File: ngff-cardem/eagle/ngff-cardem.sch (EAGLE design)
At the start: 143 parts, among them IC201 CB3Q3244PW, IC202 CB3Q3244PW, IC203 IP4234CZ6, IC204 FPF2109, IC205 FPF2109, IC301 TPS22958N-DGN, IC302 TPS22958N-DGK, J301 PJ-002BH-SMT-TR, M2 MENTOR_12701001, M3 MENTOR_12701001, Q201 12MHz, T101 BC850, T102 BC850, U201 IP4234CZ6, U202 AT91SAM3S-AU, U301 MIC5366-1.8YC5, X101 PINHD-2X3-SP, X102 ZX360D-B-10P(30), X201 MINI-USB-SHIELD-UX60-MB-5ST, X202 2.54mm, X203 JACK2.5_SJ-2523, X301 171826-4-RA

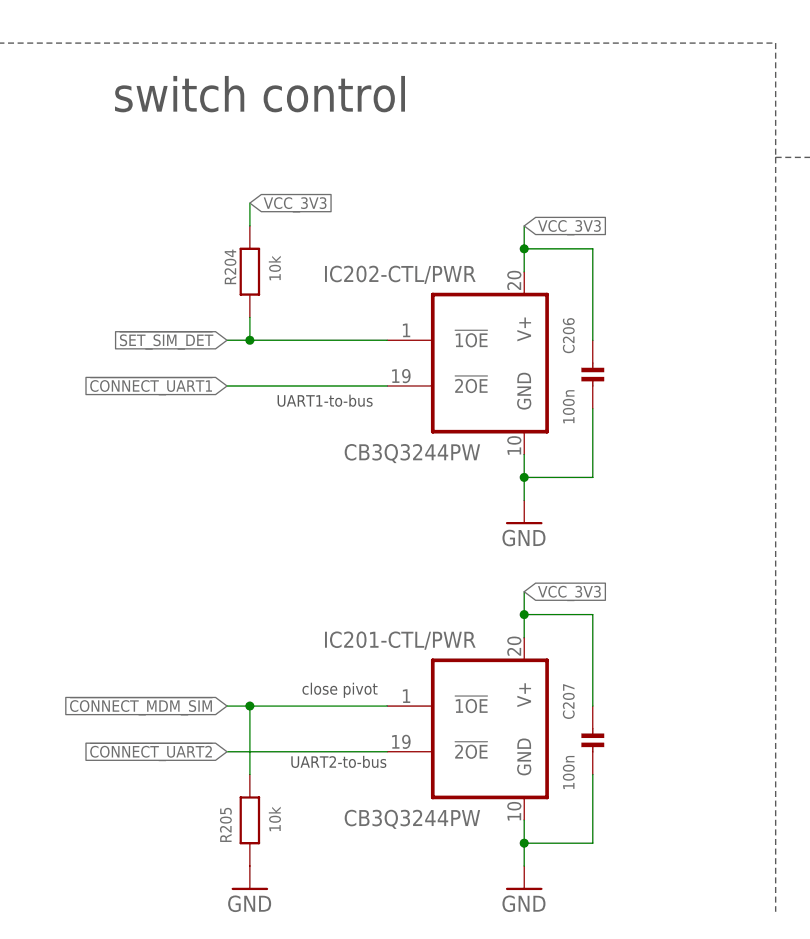
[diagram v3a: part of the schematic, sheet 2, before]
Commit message: ngff-cardem: insert 2 PUs as DNP for possible !CONNECT_UART{1,2} biasing
solves SYS#5532
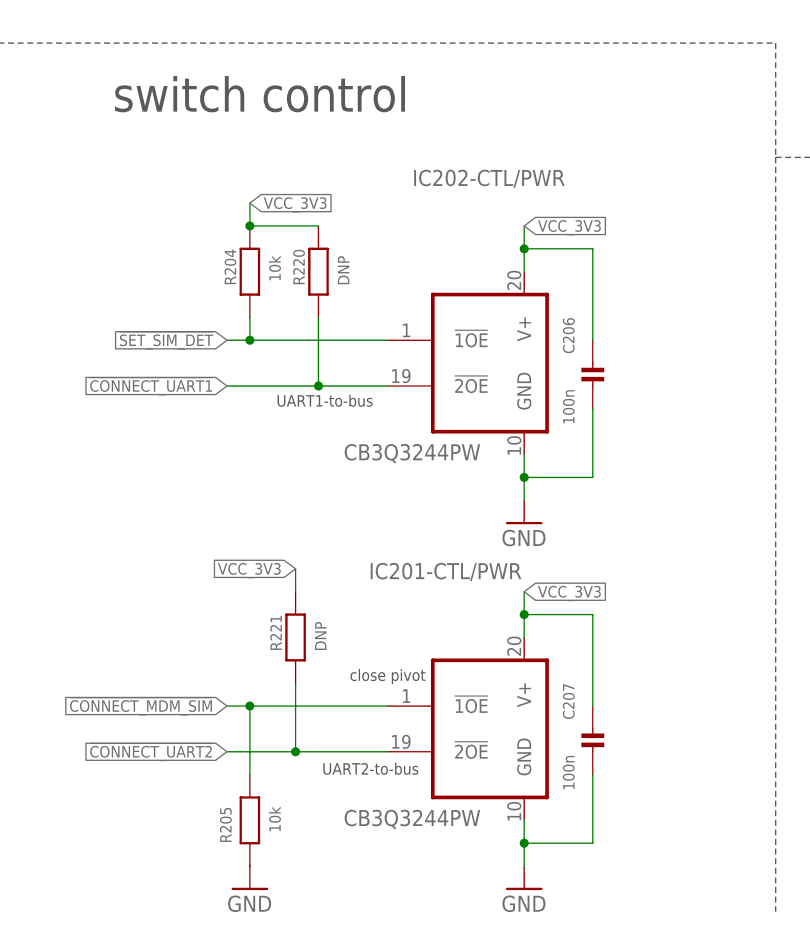
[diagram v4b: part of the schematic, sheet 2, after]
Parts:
- added R220, R221: DNP, rc-sysmocom:RESISTOR_0603
- X201: DESCRIPTION (none) -> NO DESCRIPTION; MANUFACTURER (none) -> UNKNOWN MANUFACTURER; MANUFACTURERPARTNUMBER (none) -> UNKNOWN MANUFACTURER PART NUMBER; ROHSCERTIFICATE (none) -> UNKNOWN ROHS CERTIFICATE; SOURCEPARTNUMBER (none) -> UNKNOWN SOURCE PART NUMBER
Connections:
- net !CONNECT_UART1: now also R220.2
- net !CONNECT_UART2: now also R221.2
- net VCC_3V3: now also R220.1, R221.1
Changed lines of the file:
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@@
 <part name="X201" library="con-hirose" deviceset="MINI-USB-SHIELD-" device="UX60-MB-5ST">
 <attribute name="CLASS" value="CONNECTOR"/>
-<attribute name="DESCRIPTION" value=""/>
+<attribute name="DESCRIPTION" value="NO DESCRIPTION"/>
 <attribute name="LINK" value="http://www.digikey.com/product-detail/en/hirose-electric-co-ltd/UX60-MB-5ST/H2959CT-ND/597538"/>
-<attribute name="MANUFACTURER" value=""/>
-<attribute name="MANUFACTURERPARTNUMBER" value=""/>
+<attribute name="MANUFACTURER" value="UNKNOWN MANUFACTURER"/>
+<attribute name="MANUFACTURERPARTNUMBER" value="UNKNOWN MANUFACTURER PART NUMBER"/>
 <attribute name="OC_FARNELL" value=""/>
 <attribute name="OC_NEWARK" value=""/>
 <attribute name="POPULATED" value="TRUE"/>
-<attribute name="ROHSCERTIFICATE" value=""/>
+<attribute name="ROHSCERTIFICATE" value="UNKNOWN ROHS CERTIFICATE"/>
 <attribute name="SOURCE" value="DIGIKEY"/>
-<attribute name="SOURCEPARTNUMBER" value=""/>
+<attribute name="SOURCEPARTNUMBER" value="UNKNOWN SOURCE PART NUMBER"/>
 </part>
 <part name="U201" library="laforge" deviceset="IP4234CZ6" device="">
@@
 <attribute name="SOURCEPARTNUMBER" value="UNKNOWN SOURCE PART NUMBER"/>
 </part>
+<part name="R220" library="rc-sysmocom" deviceset="RESISTOR" device="_0603" value="DNP">
+<attribute name="CLASS" value="RESISTOR"/>
+<attribute name="DESCRIPTION" value="NO DESCRIPTION"/>
+<attribute name="LINK" value="UNKNOWN LINK"/>
+<attribute name="MANUFACTURER" value="UNKNOWN MANUFACTURER"/>
+<attribute name="MANUFACTURERPARTNUMBER" value="UNKNOWN MANUFACTURER PART NUMBER"/>
+<attribute name="POPULATED" value="FALSE"/>
+<attribute name="ROHSCERTIFICATE" value="UNKNOWN ROHS CERTIFICATE"/>
+<attribute name="SOURCE" value="UNKNOWN SOURCE"/>
+<attribute name="SOURCEPARTNUMBER" value="UNKNOWN SOURCE PART NUMBER"/>
+</part>
+<part name="R221" library="rc-sysmocom" deviceset="RESISTOR" device="_0603" value="DNP">
+<attribute name="CLASS" value="RESISTOR"/>
+<attribute name="DESCRIPTION" value="NO DESCRIPTION"/>
+<attribute name="LINK" value="UNKNOWN LINK"/>
+<attribute name="MANUFACTURER" value="UNKNOWN MANUFACTURER"/>
+<attribute name="MANUFACTURERPARTNUMBER" value="UNKNOWN MANUFACTURER PART NUMBER"/>
+<attribute name="POPULATED" value="FALSE"/>
+<attribute name="ROHSCERTIFICATE" value="UNKNOWN ROHS CERTIFICATE"/>
+<attribute name="SOURCE" value="UNKNOWN SOURCE"/>
+<attribute name="SOURCEPARTNUMBER" value="UNKNOWN SOURCE PART NUMBER"/>
+</part>
 </parts>
 <sheets>
@@
 <text x="137.16" y="81.28" size="3.81" layer="97" ratio="10">switch bank</text>
 <text x="82.296" y="62.484" size="1.27" layer="97" rot="R180">UART1-to-bus</text>
-<text x="83.82" y="22.352" size="1.27" layer="97" rot="R180">UART2-to-bus</text>
-<text x="82.804" y="30.48" size="1.27" layer="97" rot="R180">close pivot</text>
+<text x="87.376" y="21.59" size="1.27" layer="97" rot="R180">UART2-to-bus</text>
+<text x="88.138" y="32.004" size="1.27" layer="97" rot="R180">close pivot</text>
 <wire x1="251.46" y1="88.9" x2="330.2" y2="88.9" width="0.1524" layer="97" style="longdash"/>
 <wire x1="134.62" y1="50.8" x2="325.12" y2="50.8" width="0.1016" layer="97" style="dashdot"/>
@@
 <instance part="GND7" gate="1" x="119.38" y="223.52" rot="R270"/>
 <instance part="GND8" gate="1" x="119.38" y="218.44" rot="R270"/>
-<instance part="IC202" gate="-CTL/PWR" x="93.98" y="66.04"/>
+<instance part="IC202" gate="-CTL/PWR" x="93.98" y="66.04" smashed="yes">
+<attribute name="NAME" x="86.614" y="85.725" size="1.778" layer="95"/>
+<attribute name="VALUE" x="94.234" y="57.023" size="1.778" layer="96" rot="R180"/>
+</instance>
 <instance part="IC202" gate="-1OE_4" x="190.5" y="10.16"/>
 <instance part="IC202" gate="-2OE_1" x="160.02" y="55.88" smashed="yes" rot="MR180">
@@
 <attribute name="NAME" x="155.702" y="48.387" size="1.778" layer="95" rot="R180"/>
 </instance>
-<instance part="IC201" gate="-CTL/PWR" x="93.98" y="25.4"/>
+<instance part="IC201" gate="-CTL/PWR" x="93.98" y="25.4" smashed="yes">
+<attribute name="NAME" x="98.806" y="43.815" size="1.778" layer="95" rot="R180"/>
+<attribute name="VALUE" x="94.234" y="16.383" size="1.778" layer="96" rot="R180"/>
+</instance>
 <instance part="IC201" gate="-1OE_2" x="198.12" y="43.18" smashed="yes">
 <attribute name="NAME" x="198.882" y="49.657" size="1.778" layer="95" rot="R180"/>
@@
 <attribute name="VALUE" x="70.739" y="77.978" size="1.27" layer="96" rot="R270"/>
 </instance>
+<instance part="R220" gate="G$1" x="76.2" y="76.2" smashed="yes" rot="R270">
+<attribute name="NAME" x="73.406" y="78.74" size="1.27" layer="95" rot="R270"/>
+<attribute name="VALUE" x="78.359" y="77.978" size="1.27" layer="96" rot="R270"/>
+<attribute name="DESCRIPTION" x="76.2" y="76.2" size="1.778" layer="96" rot="R270" display="off"/>
+<attribute name="MANUFACTURER" x="76.2" y="76.2" size="1.778" layer="96" rot="R270" display="off"/>
+<attribute name="MANUFACTURERPARTNUMBER" x="76.2" y="76.2" size="1.778" layer="96" rot="R270" display="off"/>
+<attribute name="SOURCE" x="76.2" y="76.2" size="1.778" layer="96" rot="R270" display="off"/>
+<attribute name="SOURCEPARTNUMBER" x="76.2" y="76.2" size="1.778" layer="96" rot="R270" display="off"/>
+<attribute name="ROHSCERTIFICATE" x="76.2" y="76.2" size="1.778" layer="96" rot="R270" display="off"/>
+<attribute name="POPULATED" x="76.2" y="76.2" size="1.778" layer="96" rot="R270" display="off"/>
+<attribute name="CLASS" x="76.2" y="76.2" size="1.778" layer="96" rot="R270" display="off"/>
+<attribute name="LINK" x="76.2" y="76.2" size="1.778" layer="96" rot="R270" display="off"/>
+</instance>
+<instance part="R221" gate="G$1" x="73.66" y="35.56" smashed="yes" rot="R270">
+<attribute name="NAME" x="70.866" y="38.1" size="1.27" layer="95" rot="R270"/>
+<attribute name="VALUE" x="75.819" y="37.338" size="1.27" layer="96" rot="R270"/>
+<attribute name="DESCRIPTION" x="73.66" y="35.56" size="1.778" layer="96" rot="R270" display="off"/>
+<attribute name="MANUFACTURER" x="73.66" y="35.56" size="1.778" layer="96" rot="R270" display="off"/>
+<attribute name="MANUFACTURERPARTNUMBER" x="73.66" y="35.56" size="1.778" layer="96" rot="R270" display="off"/>
+<attribute name="SOURCE" x="73.66" y="35.56" size="1.778" layer="96" rot="R270" display="off"/>
+<attribute name="SOURCEPARTNUMBER" x="73.66" y="35.56" size="1.778" layer="96" rot="R270" display="off"/>
+<attribute name="ROHSCERTIFICATE" x="73.66" y="35.56" size="1.778" layer="96" rot="R270" display="off"/>
+<attribute name="POPULATED" x="73.66" y="35.56" size="1.778" layer="96" rot="R270" display="off"/>
+<attribute name="CLASS" x="73.66" y="35.56" size="1.778" layer="96" rot="R270" display="off"/>
+<attribute name="LINK" x="73.66" y="35.56" size="1.778" layer="96" rot="R270" display="off"/>
+</instance>
 </instances>
 <busses>
@@
 <label x="66.04" y="63.5" size="1.27" layer="95" rot="R180" xref="yes"/>
 <pinref part="IC202" gate="-CTL/PWR" pin="!2OE"/>
-<wire x1="83.82" y1="63.5" x2="66.04" y2="63.5" width="0.1524" layer="91"/>
+<wire x1="83.82" y1="63.5" x2="76.2" y2="63.5" width="0.1524" layer="91"/>
+<pinref part="R220" gate="G$1" pin="2"/>
+<wire x1="76.2" y1="63.5" x2="66.04" y2="63.5" width="0.1524" layer="91"/>
+<wire x1="76.2" y1="71.12" x2="76.2" y2="63.5" width="0.1524" layer="91"/>
+<junction x="76.2" y="63.5"/>
 </segment>
 <segment>
@@
 <wire x1="68.58" y1="81.28" x2="68.58" y2="83.82" width="0.1524" layer="91"/>
 <label x="68.58" y="83.82" size="1.27" layer="95" xref="yes"/>
+<pinref part="R220" gate="G$1" pin="1"/>
+<wire x1="76.2" y1="81.28" x2="68.58" y2="81.28" width="0.1524" layer="91"/>
+<junction x="68.58" y="81.28"/>
 </segment>
 <segment>
@@
 <label x="30.48" y="66.04" size="1.27" layer="95" rot="R90" xref="yes"/>
 </segment>
+<segment>
+<label x="73.66" y="43.18" size="1.27" layer="95" rot="R180" xref="yes"/>
+<pinref part="R221" gate="G$1" pin="1"/>
+<wire x1="73.66" y1="43.18" x2="73.66" y2="40.64" width="0.1524" layer="91"/>
+</segment>
 </net>
 <net name="N$45" class="0">
@@
 <segment>
 <pinref part="IC201" gate="-CTL/PWR" pin="!2OE"/>
-<wire x1="83.82" y1="22.86" x2="66.04" y2="22.86" width="0.1524" layer="91"/>
+<wire x1="83.82" y1="22.86" x2="73.66" y2="22.86" width="0.1524" layer="91"/>
 <label x="66.04" y="22.86" size="1.27" layer="95" rot="R180" xref="yes"/>
+<pinref part="R221" gate="G$1" pin="2"/>
+<wire x1="73.66" y1="22.86" x2="66.04" y2="22.86" width="0.1524" layer="91"/>
+<wire x1="73.66" y1="30.48" x2="73.66" y2="22.86" width="0.1524" layer="91"/>
+<junction x="73.66" y="22.86"/>
 </segment>
 </net>
